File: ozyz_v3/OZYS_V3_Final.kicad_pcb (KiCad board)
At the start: 4 copper layers, 117 parts, among them CN1 532610571, J2 Conn_01x02_Pin, J3 AudioJack4, J4 AudioJack4, J5 AudioJack4, J6 AudioJack4, Q1 AO3400A, Q10 2N7002, Q2 AO3401A, Q3 2N7002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

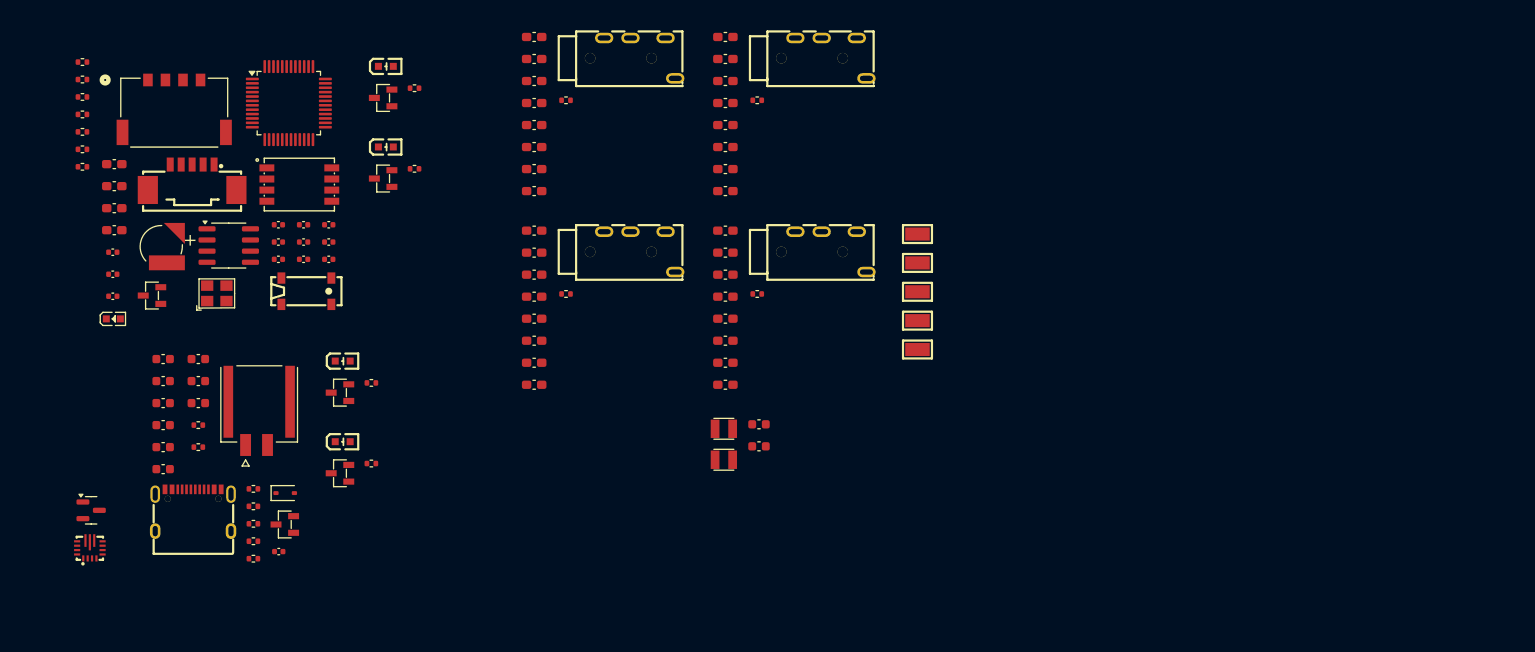
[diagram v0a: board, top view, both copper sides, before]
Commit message: update connector placement
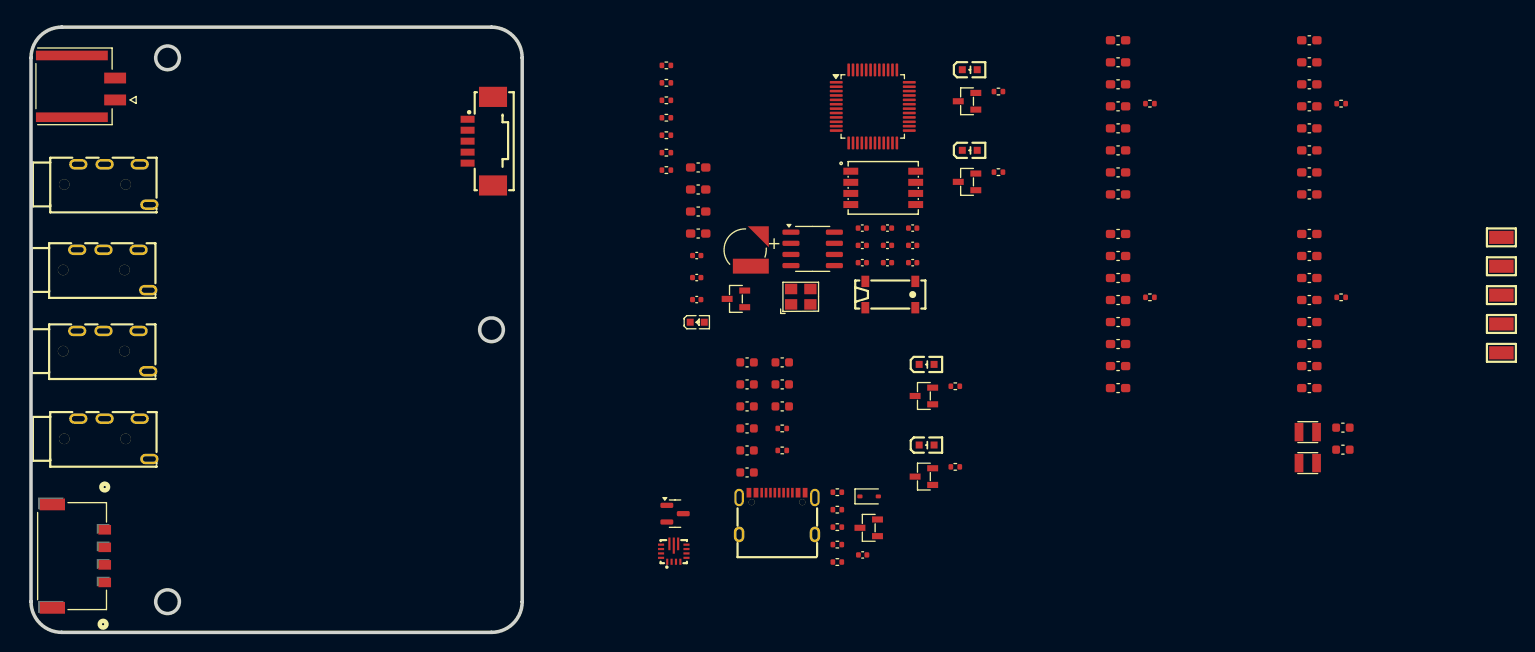
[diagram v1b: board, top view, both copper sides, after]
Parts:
- added J_CAN2: 2053380004, Rocketry_Manual:CONN_2053380000-SD_04_MOL, B.Cu at (24.4, 78.7)
- moved J4 85.4 mm to (29.2, 46.2)
- moved J6 82.7 mm to (29.2, 55.4)
- moved C2 66.6 mm to (143.9, 42.1)
- moved C26 66.6 mm to (143.9, 20.0)
- moved C27 66.6 mm to (143.9, 22.5)
- moved C30 66.6 mm to (143.9, 47.1)
- moved C32 66.6 mm to (143.9, 25.0)
- moved C34 66.6 mm to (143.9, 49.6)
- moved C36 66.6 mm to (143.9, 27.5)
- moved C7 66.6 mm to (143.9, 44.6)
- moved LED1 66.6 mm to (122.0, 66.1)
- moved LED3 66.6 mm to (122.0, 57.0)
- moved Q10 66.6 mm to (126.7, 36.1)
- moved Q4 66.6 mm to (121.7, 69.7)
- moved Q6 66.6 mm to (126.7, 26.9)
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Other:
- board outline added: 56 x 69 mm

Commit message: Epsilon PCB Finished
Updated OZYS still WIP.
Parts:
- moved R18 141.8 mm to (28.2, 41.8), turned to -90 degrees
- moved R33 141.1 mm to (28.2, 51.0), turned to -90 degrees
- moved R20 130.9 mm to (36.0, 48.0), turned to 90 degrees
- moved R29 129.8 mm to (36.0, 44.2), turned to -90 degrees
- moved R23 129.8 mm to (36.0, 57.2), turned to 90 degrees
- moved R35 129.7 mm to (36.0, 53.5), turned to -90 degrees
- moved C35 129.5 mm to (37.8, 48.0), turned to -90 degrees
- moved C31 129.4 mm to (37.8, 44.2), turned to -90 degrees
- moved C37 128.1 mm to (37.8, 57.2), turned to -90 degrees
- moved C33 128.1 mm to (37.8, 53.5), turned to -90 degrees
- moved C24 127.0 mm to (41.2, 48.0), turned to 90 degrees
- moved R24 126.8 mm to (39.5, 48.0), turned to -90 degrees
- moved C22 126.8 mm to (41.2, 44.2), turned to 90 degrees
- moved R21 126.7 mm to (39.5, 44.2), turned to 90 degrees
- moved R36 126.2 mm to (39.5, 57.2), turned to -90 degrees
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
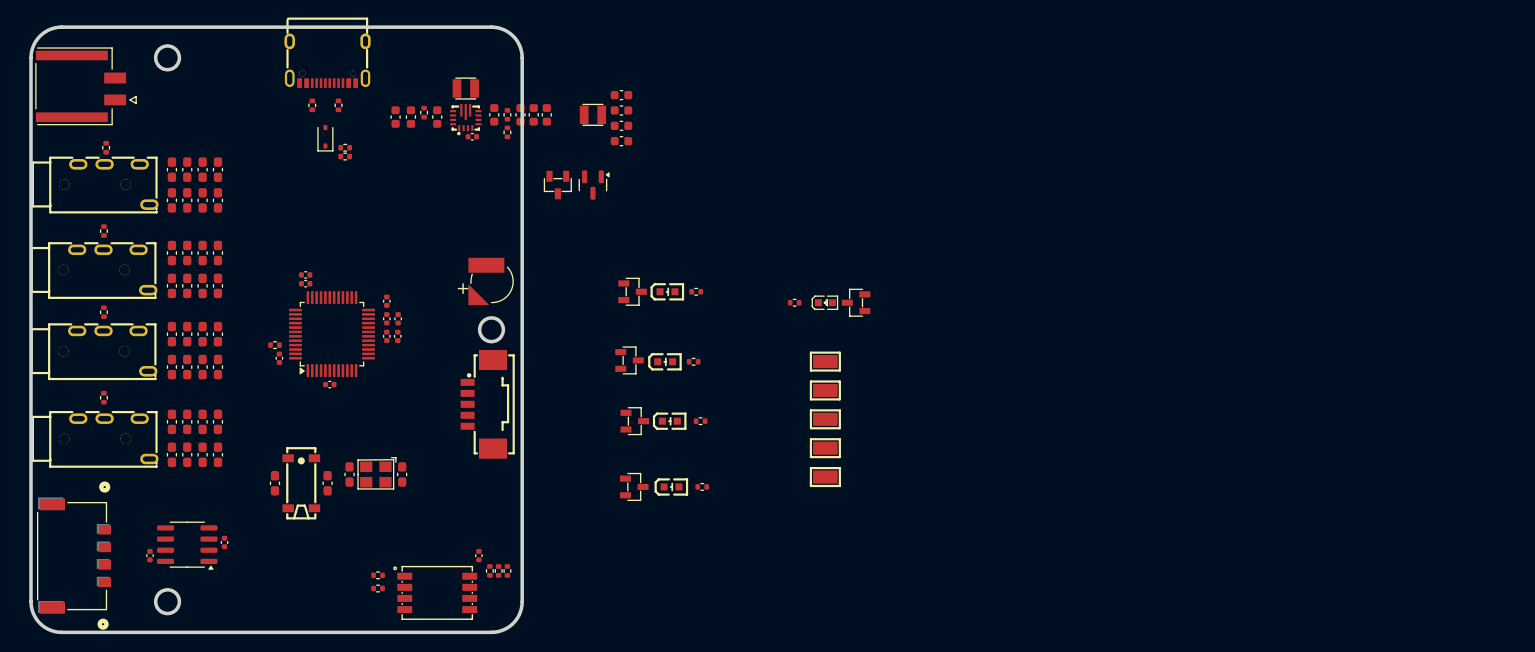
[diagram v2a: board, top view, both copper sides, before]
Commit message: Saving Rough Iteration of Ozys V3
-STM Pins to be configured with current layout
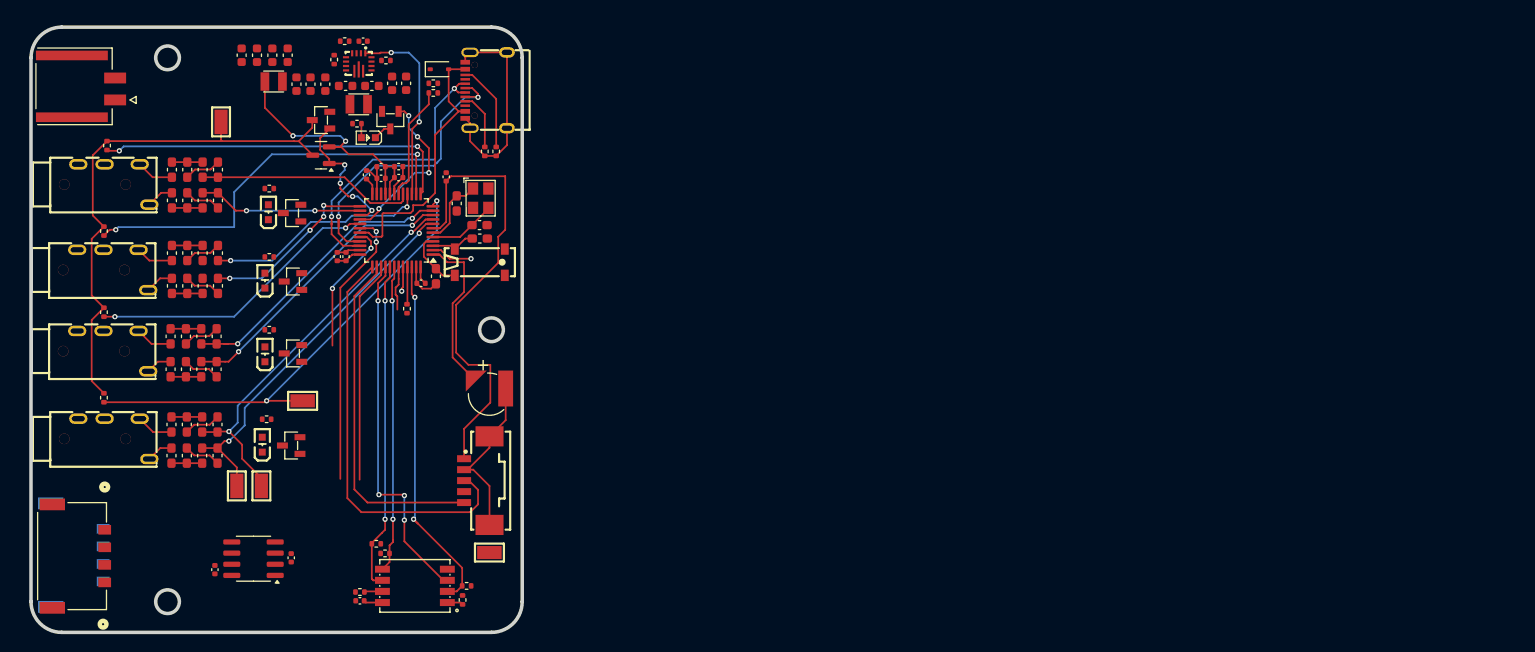
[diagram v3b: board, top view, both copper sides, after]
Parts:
- moved U8 78.3 mm to (41.6, 29.3), turned to 90 degrees
- moved U5 68.6 mm to (43.4, 70.8), turned to -90 degrees
- moved U6 65.2 mm to (46.2, 70.8), turned to -90 degrees
- moved U7 59.6 mm to (50.9, 61.1)
- moved Q3 57.0 mm to (60.9, 29.1), turned to 90 degrees
- moved LED5 55.4 mm to (58.4, 31.1), turned to 180 degrees
- moved R1 53.9 mm to (57.1, 29.5)
- moved R17 52.3 mm to (47.1, 36.9)
- moved R32 50.3 mm to (47.1, 53.0)
- moved R15 50.3 mm to (46.8, 63.2)
- moved R26 48.8 mm to (47.1, 44.7)
- moved LED1 48.3 mm to (47.0, 39.6), turned to 90 degrees
- moved LED2 46.9 mm to (46.3, 66.1), turned to 90 degrees
- moved LED4 46.8 mm to (46.6, 55.8), turned to 90 degrees
- moved LED3 45.9 mm to (46.6, 47.4), turned to 90 degrees
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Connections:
- U2 pad 10: unconnected-(U2-PA2-Pad10) -> /DP4
- U2 pad 11: unconnected-(U2-PA3-Pad11) -> /DM4
- U2 pad 12: unconnected-(U2-PA4-Pad12) -> /ONE_WIRE_OUT1
- U2 pad 13: unconnected-(U2-PA5-Pad13) -> /ONE_WIRE_OUT3
- U2 pad 14: unconnected-(U2-PA6-Pad14) -> /ONE_WIRE_OUT2
- U2 pad 15: unconnected-(U2-PA7-Pad15) -> /PS
- U2 pad 16: unconnected-(U2-PB0-Pad16) -> /DM2
- U2 pad 17: unconnected-(U2-PB1-Pad17) -> /DM3
- U2 pad 18: unconnected-(U2-PB2-Pad18) -> /BAT_V_M
- U2 pad 25: unconnected-(U2-PB11-Pad25) -> /DP2
- U2 pad 26: unconnected-(U2-PB12-Pad26) -> /DP3
- U2 pad 27: unconnected-(U2-PB13-Pad27) -> /3V3A_SW_EN
- U2 pad 28: unconnected-(U2-PB14-Pad28) -> /STATUS_LED
- U2 pad 29: unconnected-(U2-PB15-Pad29) -> /ONE_WIRE_OUT4
- U2 pad 46: unconnected-(U2-PB9-Pad46) -> /CS
- U2 pad 8: unconnected-(U2-PA0-Pad8) -> /DP1
- U2 pad 9: unconnected-(U2-PA1-Pad9) -> /DM1
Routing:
- net GND: track 0.00 -> 93.1 mm
- net 3V3A_SW: track 0.00 -> 61.7 mm
- net /ONE_WIRE_OUT1: track 0.00 -> 54.4 mm, vias 0 -> 2
- net /nRST: track 0.00 -> 52.2 mm
- net /SWDIO: track 0.00 -> 47.2 mm
- net /ONE_WIRE_OUT2: track 0.00 -> 46.5 mm, vias 0 -> 2
- net /DM1: track 0.00 -> 45.2 mm, vias 0 -> 2
- net /DP1: track 0.00 -> 43.5 mm, vias 0 -> 2
- net /ONE_WIRE_OUT3: track 0.00 -> 41.4 mm, vias 0 -> 2
- net /MKDV32_Clock: track 0.00 -> 41.3 mm, vias 0 -> 4
- net /CS: track 0.00 -> 41.2 mm, vias 0 -> 2
- net /SWDCLK: track 0.00 -> 39.5 mm
- net /MKDV32_Output: track 0.00 -> 37.9 mm, vias 0 -> 2
- net /USB_DN: track 0.00 -> 35.2 mm, vias 0 -> 2
- net /MKDV32_Input: track 0.00 -> 35.2 mm, vias 0 -> 2
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- added copper zone on In1.Cu, net GND
- added copper zone on In2.Cu, net GND

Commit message: Saving another rough trace
saving for iteration purposes
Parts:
- moved U9 22.9 mm to (50.7, 70.6)
- moved R5 0.32 mm to (69.9, 82.1)
- moved R4 0.27 mm to (69.4, 83.8)
- moved Q6 0.22 mm to (49.7, 66.0)
- moved R15 0.22 mm to (46.9, 63.0)
- moved LED2 0.22 mm to (46.4, 65.9)
- moved R2 0.20 mm to (59.3, 77.2)
- moved R3 0.20 mm to (60.3, 78.3)
- moved C39 0.10 mm to (71.0, 42.6)
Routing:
- net Net-(J_CAN1-Pin_1): track 0.00 -> 42.6 mm, vias 0 -> 2
- net Net-(D2-K): track 0.00 -> 39.5 mm
- net Net-(J_CAN1-Pin_2): track 0.00 -> 30.0 mm, vias 0 -> 1
- net Net-(J_CAN1-Pin_3): track 0.00 -> 27.7 mm, vias 0 -> 1
- net Net-(J_CAN1-Pin_4): track 0.00 -> 26.3 mm, vias 0 -> 1
- net /CAN_TXD: track 25.3 -> 33.2 mm
- net /CAN_RXD: track 31.9 -> 39.0 mm
- net +3V3: track 6.94 -> 9.56 mm
- net GND: track 93.1 -> 95.5 mm
- net /ONE_WIRE_OUT1: track 54.4 -> 55.2 mm, vias 2 -> 4
- net /nRST: track 52.2 -> 51.7 mm

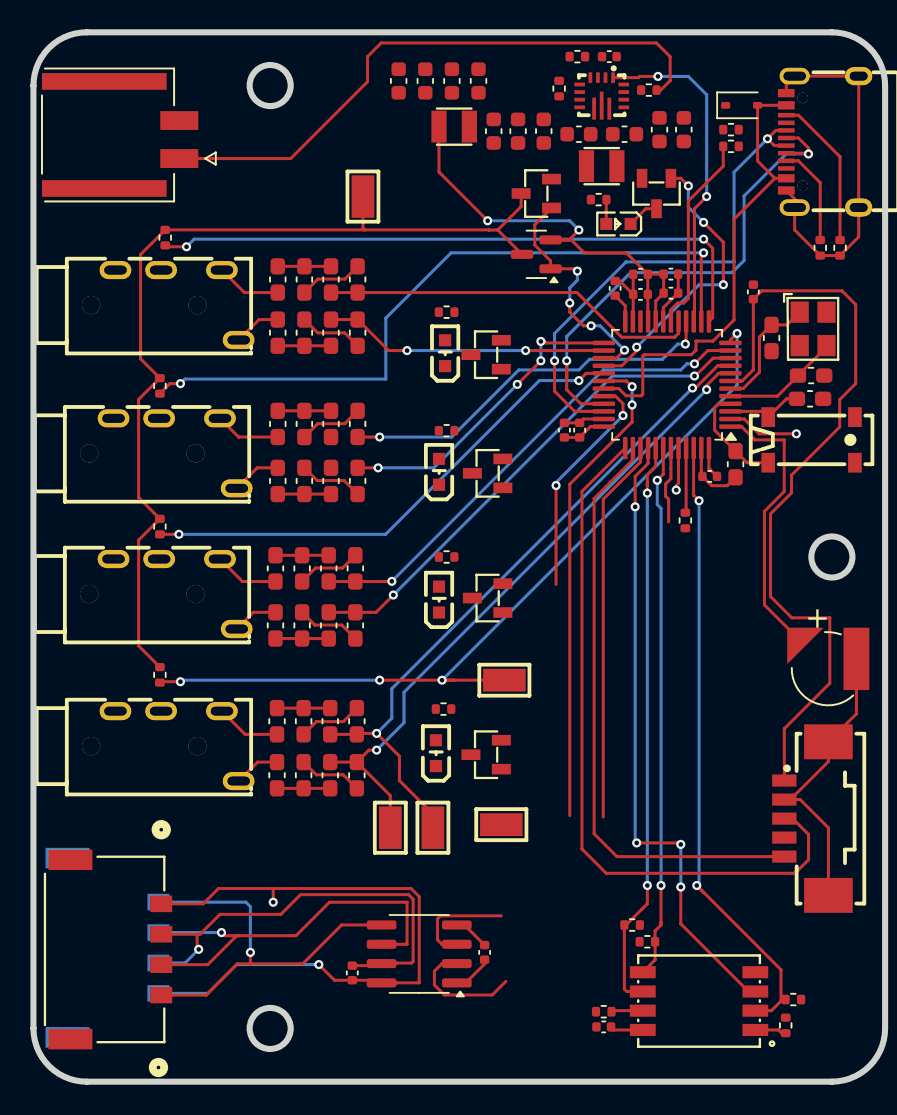
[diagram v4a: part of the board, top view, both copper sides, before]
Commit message: Fixed LEDs
- Just need to clean it up then add pours and GND vias
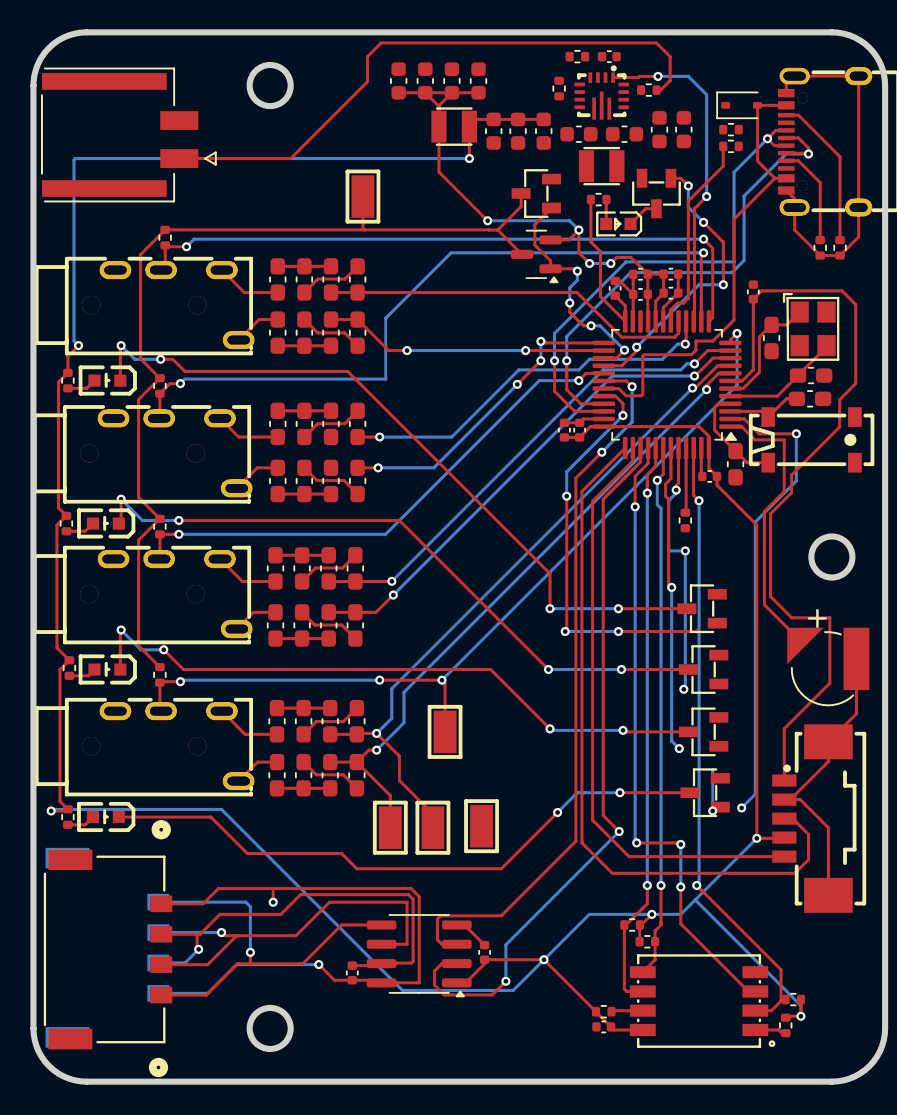
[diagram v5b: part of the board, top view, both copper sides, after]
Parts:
- moved R32 25.9 mm to (22.3, 60.3), turned to -90 degrees
- moved R26 25.7 mm to (22.1, 50.8), turned to -90 degrees
- moved R15 25.7 mm to (22.2, 70.1), turned to -90 degrees
- moved R17 25.3 mm to (22.2, 41.4), turned to -90 degrees
- moved LED4 22.3 mm to (24.8, 60.4), turned to 180 degrees
- moved LED1 22.3 mm to (24.8, 41.4), turned to 180 degrees
- moved LED3 22.2 mm to (24.7, 50.8), turned to 180 degrees
- moved LED2 22.1 mm to (24.7, 70.1), turned to 180 degrees
- moved Q4 21.9 mm to (63.9, 56.4)
- moved Q8 19.2 mm to (64.0, 60.4)
- moved Q10 16.7 mm to (64.0, 64.5)
- moved Q6 14.6 mm to (64.1, 68.5)
- moved U7 5.17 mm to (47.0, 64.5), turned to 90 degrees
- moved U9 1.30 mm to (49.4, 70.7), turned to -90 degrees
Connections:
- C13 pad 2: +3.3V -> +3V3
- U3 pad 8: +3.3V -> +3V3
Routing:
- net +3V3: track 9.56 -> 216.3 mm, vias 0 -> 7
- net Net-(LED1-K): track 0.00 -> 48.2 mm, vias 0 -> 4
- net Net-(LED3-K): track 0.00 -> 43.6 mm, vias 0 -> 4
- net Net-(LED4-K): track 0.00 -> 42.7 mm, vias 0 -> 4
- net Net-(LED2-K): track 0.00 -> 41.0 mm, vias 0 -> 2
- net unconnected-(U2-PC13-Pad2): track 4.74 -> 30.8 mm, vias 1 -> 2
- net /CAN_TXD: track 33.2 -> 50.6 mm, vias 0 -> 2
- net unconnected-(U2-PB6-Pad43): track 5.09 -> 20.3 mm, vias 0 -> 2
- net unconnected-(U2-PB7-Pad44): track 2.82 -> 17.3 mm, vias 1 -> 3
- net unconnected-(U2-PA10-Pad32): track 15.2 -> 26.8 mm, vias 2 -> 4
- net +3V3A: track 30.7 -> 41.8 mm, vias 2 -> 4
- net /CAN_RXD: track 39.0 -> 47.4 mm
- net /LED1: track 0.00 -> 2.80 mm, vias 0 -> 1
- net GND: track 95.5 -> 92.8 mm
- net +3.3V: track 2.17 -> 0.00 mm
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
